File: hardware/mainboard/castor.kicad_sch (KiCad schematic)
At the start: 46 parts, among them J116 OSC, Q1 MMBT3906, U3 TL074, U4 74LVC2G74, U5 MCP6001-OT, U6 TL074

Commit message: Cleanup MCU schematic
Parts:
- C11: Reqs audio path, 20v -> audio path, low-voltage (3.3V), 16V; finalized yes & alt -> (none); mpn CL21A106KAYNNN -> (none); mpn alt CL21A106KAFN3NE -> (none); mpn specs 10% 25v -> (none)
- C12: Reqs audio path, 20v -> audio path, low-voltage (3.3V), 16V; finalized yes & alt -> no; mpn CL21A106KAYNNN -> (none); mpn alt CL21A106KAFN3NE -> (none); mpn specs 10% 25v -> (none)
- C13: Reqs audio path, 20v -> audio path, low-voltage (3.3V), 16V; mpn CL21A106KAYNNN -> (none); mpn alt CL21A106KAFN3NE -> (none); mpn specs 10% 25v -> (none)
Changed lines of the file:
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@@
     (rev "v5")
     (company "Winterbloom")
-    (comment 1 "CERN-OHL-P v2")
-    (comment 2 "Alethea Flowers")
+    (comment 1 "Alethea Flowers")
+    (comment 2 "CERN-OHL-P v2")
+    (comment 3 "gemini.wntr.dev")
   )
   (junction (at 207.01 111.76) (diameter 0) (color 0 0 0 0)
@@
       (effects (font (size 1.27 1.27)) hide)
     )
-    (property "finalized" "yes & alt" (id 4) (at 203.835 45.72 0)
-      (effects (font (size 1.27 1.27)) hide)
-    )
-    (property "mpn" "CL21A106KAYNNN" (id 5) (at 203.835 45.72 0)
-      (effects (font (size 1.27 1.27)) hide)
-    )
-    (property "mpn specs" "10% 25v" (id 6) (at 203.835 45.72 0)
-      (effects (font (size 1.27 1.27)) hide)
-    )
-    (property "mpn alt" "CL21A106KAFN3NE" (id 7) (at 203.835 45.72 0)
-      (effects (font (size 1.27 1.27)) hide)
-    )
-    (property "Reqs" "audio path, 20v" (id 8) (at 203.835 45.72 0)
+    (property "finalized" "" (id 4) (at 203.835 45.72 0)
+      (effects (font (size 1.27 1.27)) hide)
+    )
+    (property "mpn" "" (id 5) (at 203.835 45.72 0)
+      (effects (font (size 1.27 1.27)) hide)
+    )
+    (property "mpn specs" "" (id 6) (at 203.835 45.72 0)
+      (effects (font (size 1.27 1.27)) hide)
+    )
+    (property "mpn alt" "" (id 7) (at 203.835 45.72 0)
+      (effects (font (size 1.27 1.27)) hide)
+    )
+    (property "Reqs" "audio path, low-voltage (3.3V), 16V" (id 8) (at 203.835 45.72 0)
       (effects (font (size 1.27 1.27)) hide)
     )
@@
       (effects (font (size 1.27 1.27)) hide)
     )
-    (property "mpn" "CL21A106KAYNNN" (id 5) (at 203.2 78.74 0)
-      (effects (font (size 1.27 1.27)) hide)
-    )
-    (property "mpn specs" "10% 25v" (id 6) (at 203.2 78.74 0)
-      (effects (font (size 1.27 1.27)) hide)
-    )
-    (property "mpn alt" "CL21A106KAFN3NE" (id 7) (at 203.2 78.74 0)
-      (effects (font (size 1.27 1.27)) hide)
-    )
-    (property "Reqs" "audio path, 20v" (id 8) (at 203.2 78.74 0)
+    (property "mpn" "" (id 5) (at 203.2 78.74 0)
+      (effects (font (size 1.27 1.27)) hide)
+    )
+    (property "mpn specs" "" (id 6) (at 203.2 78.74 0)
+      (effects (font (size 1.27 1.27)) hide)
+    )
+    (property "mpn alt" "" (id 7) (at 203.2 78.74 0)
+      (effects (font (size 1.27 1.27)) hide)
+    )
+    (property "Reqs" "audio path, low-voltage (3.3V), 16V" (id 8) (at 203.2 78.74 0)
       (effects (font (size 1.27 1.27)) hide)
     )
@@
       (effects (font (size 1.27 1.27)) hide)
     )
-    (property "finalized" "yes & alt" (id 4) (at 203.2 111.76 0)
-      (effects (font (size 1.27 1.27)) hide)
-    )
-    (property "mpn" "CL21A106KAYNNN" (id 5) (at 203.2 111.76 0)
-      (effects (font (size 1.27 1.27)) hide)
-    )
-    (property "mpn specs" "10% 25v" (id 6) (at 203.2 111.76 0)
-      (effects (font (size 1.27 1.27)) hide)
-    )
-    (property "mpn alt" "CL21A106KAFN3NE" (id 7) (at 203.2 111.76 0)
-      (effects (font (size 1.27 1.27)) hide)
-    )
-    (property "Reqs" "audio path, 20v" (id 8) (at 203.2 111.76 0)
-      (effects (font (size 1.27 1.27)) hide)
-    )
+    (property "finalized" "no" (id 4) (at 203.2 111.76 0)
+      (effects (font (size 1.27 1.27)) hide)
+    )
+    (property "mpn" "" (id 5) (at 203.2 111.76 0)
+      (effects (font (size 1.27 1.27)) hide)
+    )
+    (property "mpn specs" "" (id 6) (at 203.2 111.76 0)
+      (effects (font (size 1.27 1.27)) hide)
+    )
+    (property "mpn alt" "" (id 7) (at 203.2 111.76 0)
+      (effects (font (size 1.27 1.27)) hide)
+    )
+    (property "Reqs" "audio path, low-voltage (3.3V), 16V" (id 8) (at 203.2 111.76 0)
+      (effects (font (size 1.27 1.27)) hide)
+    )

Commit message: More schematic cleanup - nearly done!
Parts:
- J116: value OSC -> OSC OUT
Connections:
- net PULSE renamed PULSE_OUT
- net RAMP renamed RAMP_OUT
- net SUB renamed SUB_OUT
- net charge_cv_in renamed CHARGE_CV_IN
- net mix_out renamed MIX_OUT
- net pwm_cv_in renamed PWM_CV_IN
- net square_in renamed SQUARE_IN
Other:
- moved on the sheet: C11, C12, C13, C14, C15, C16, R10, R11, R12, R13, R14, R15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

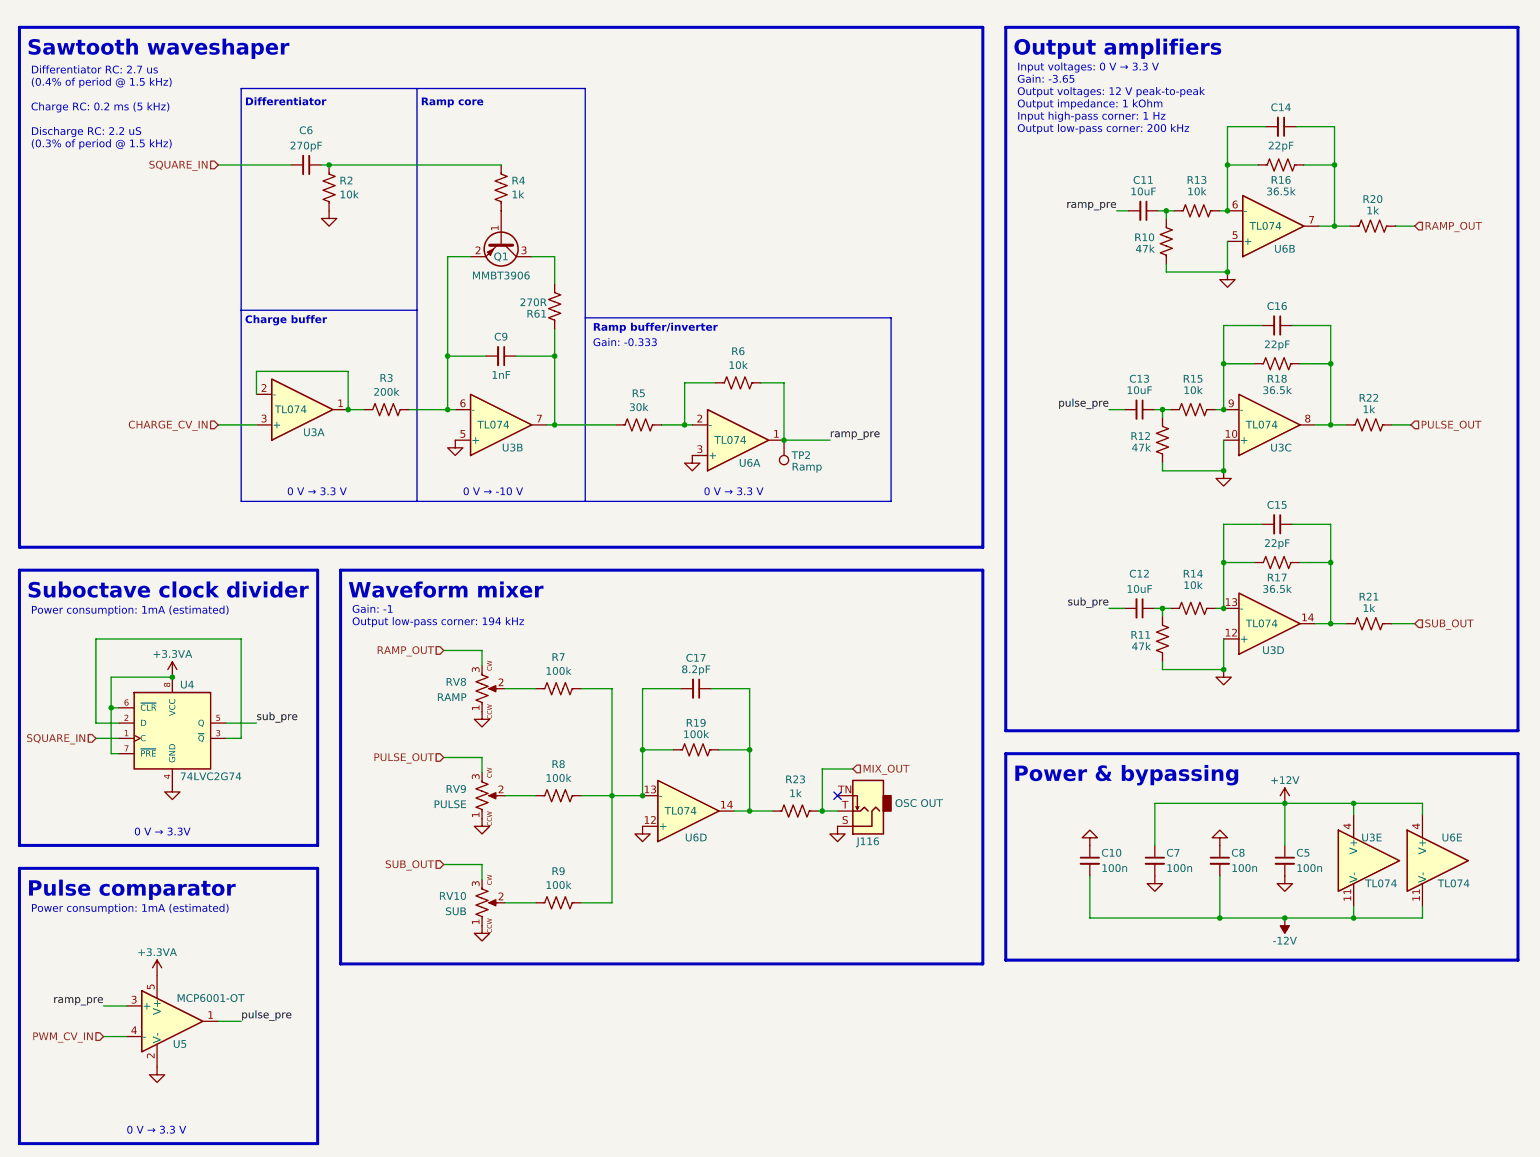
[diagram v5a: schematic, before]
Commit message: Reannotate schematic
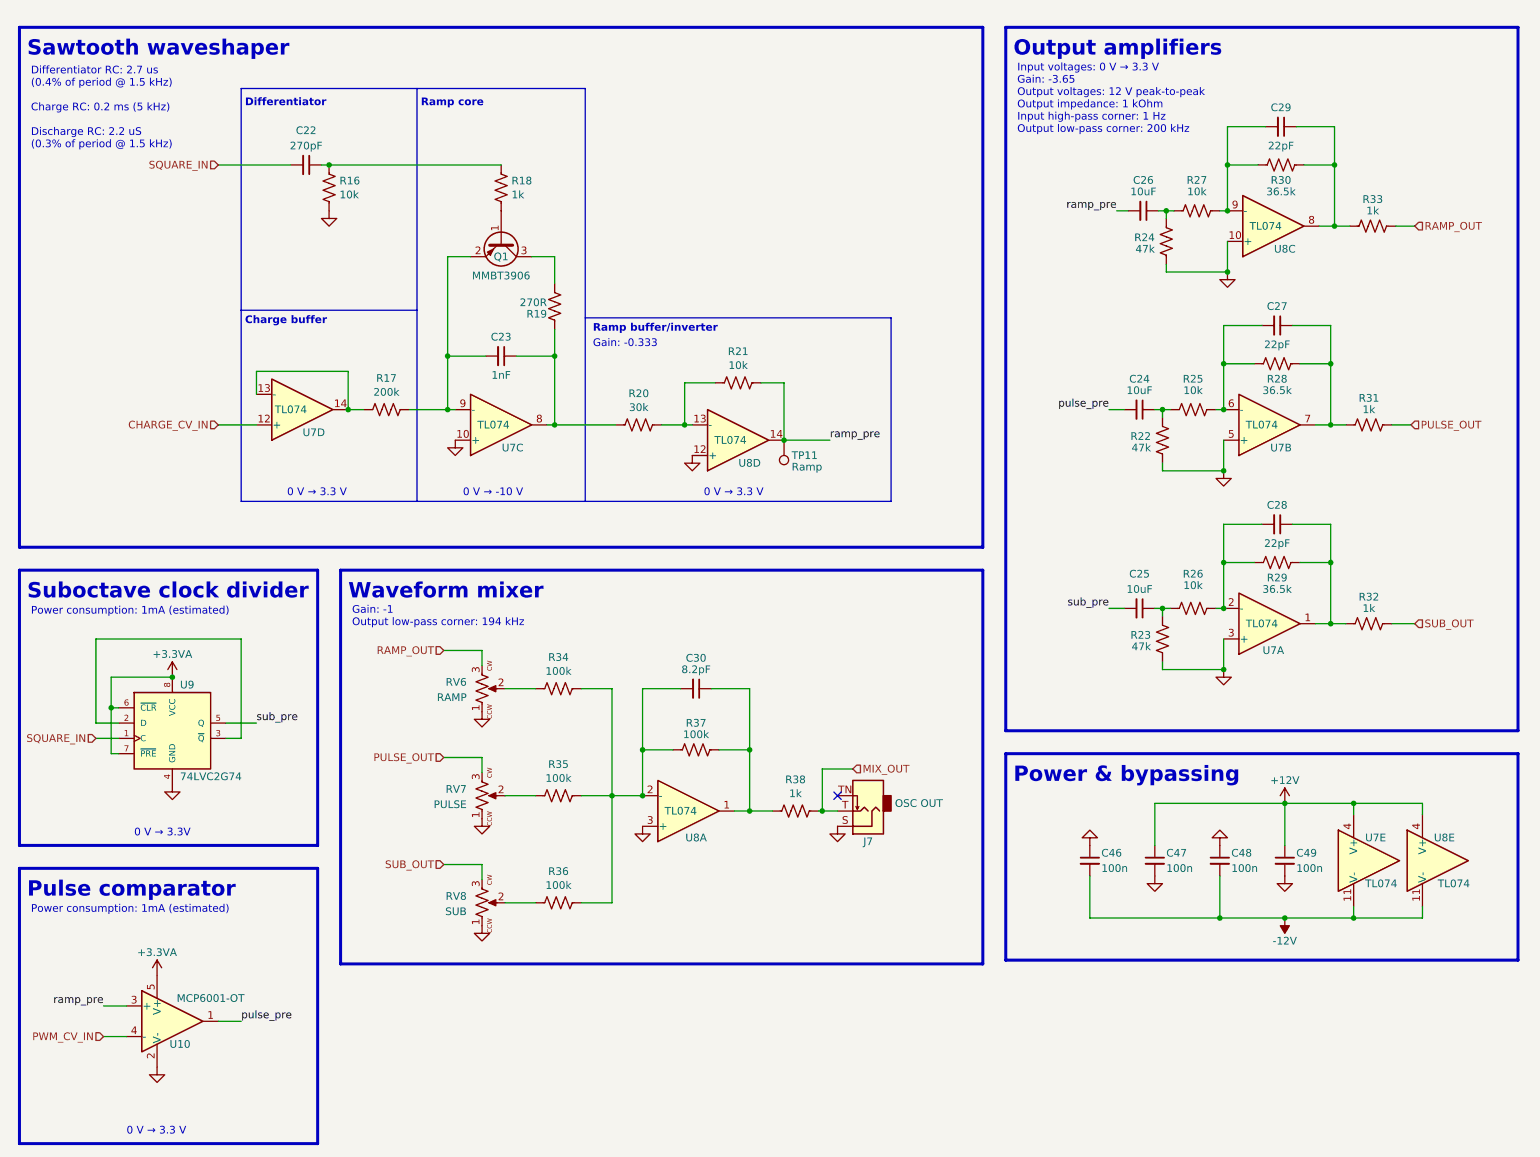
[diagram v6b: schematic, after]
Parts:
- renumbered C6 to C22, C9 to C23, C13 to C24, C12 to C25, C11 to C26, C16 to C27, C15 to C28, C14 to C29, C17 to C30, C10 to C46, C7 to C47, C8 to C48, C5 to C49, J116 to J7, R2 to R16, R3 to R17, R4 to R18, R61 to R19, R5 to R20, R6 to R21, R12 to R22, R11 to R23, R10 to R24, R15 to R25, R14 to R26, R13 to R27, R18 to R28, R17 to R29, R16 to R30, R22 to R31, R21 to R32, R20 to R33, R7 to R34, R8 to R35, R9 to R36, R19 to R37, R23 to R38, RV8 to RV6, RV9 to RV7, RV10 to RV8, TP2 to TP11, U5 to U10, U3 to U7, U6 to U8, U4 to U9
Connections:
- net CHARGE_CV_IN: now also U7.12 (+); no longer U7.3 (+)
- net GND: now also U7.10 (+), U7.3 (+), U7.5 (+), U8.10 (+), U8.12 (+), U8.3 (+); no longer U7.10 (+), U7.12 (+), U7.5 (+), U8.12 (+), U8.3 (+), U8.5 (+)
- net ramp_pre: now also U8.14; no longer U8.1
- net at C23.2, Q1.2 (E), R17.2: now also U7.9 (-); no longer U7.6 (-)
- net at C23.1, R19.1, R20.1: now also U7.8; no longer U7.7
- net at R20.2, R21.1: now also U8.13 (-); no longer U8.2 (-)
- net at C29.2, R27.2, R30.1: now also U8.9 (-); no longer U8.6 (-)
- net at C29.1, R30.2, R33.1: now also U8.8; no longer U8.7
- net at C30.2, R34.2, R35.2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: now also U8.2 (-); no longer U8.13 (-)
- net at C30.1, R37.2, R38.1: now also U8.1; no longer U8.14
- net at C27.2, R25.2, R28.1: now also U7.6 (-); no longer U7.9 (-)
- net at C27.1, R28.2, R31.1: now also U7.7; no longer U7.8
- net at C28.2, R26.2, R29.1: now also U7.2 (-); no longer U7.13 (-)
- net at C28.1, R29.2, R32.1: now also U7.1; no longer U7.14
- new net: R17.1, U7.13 (-), U7.14

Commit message: Normalize component values
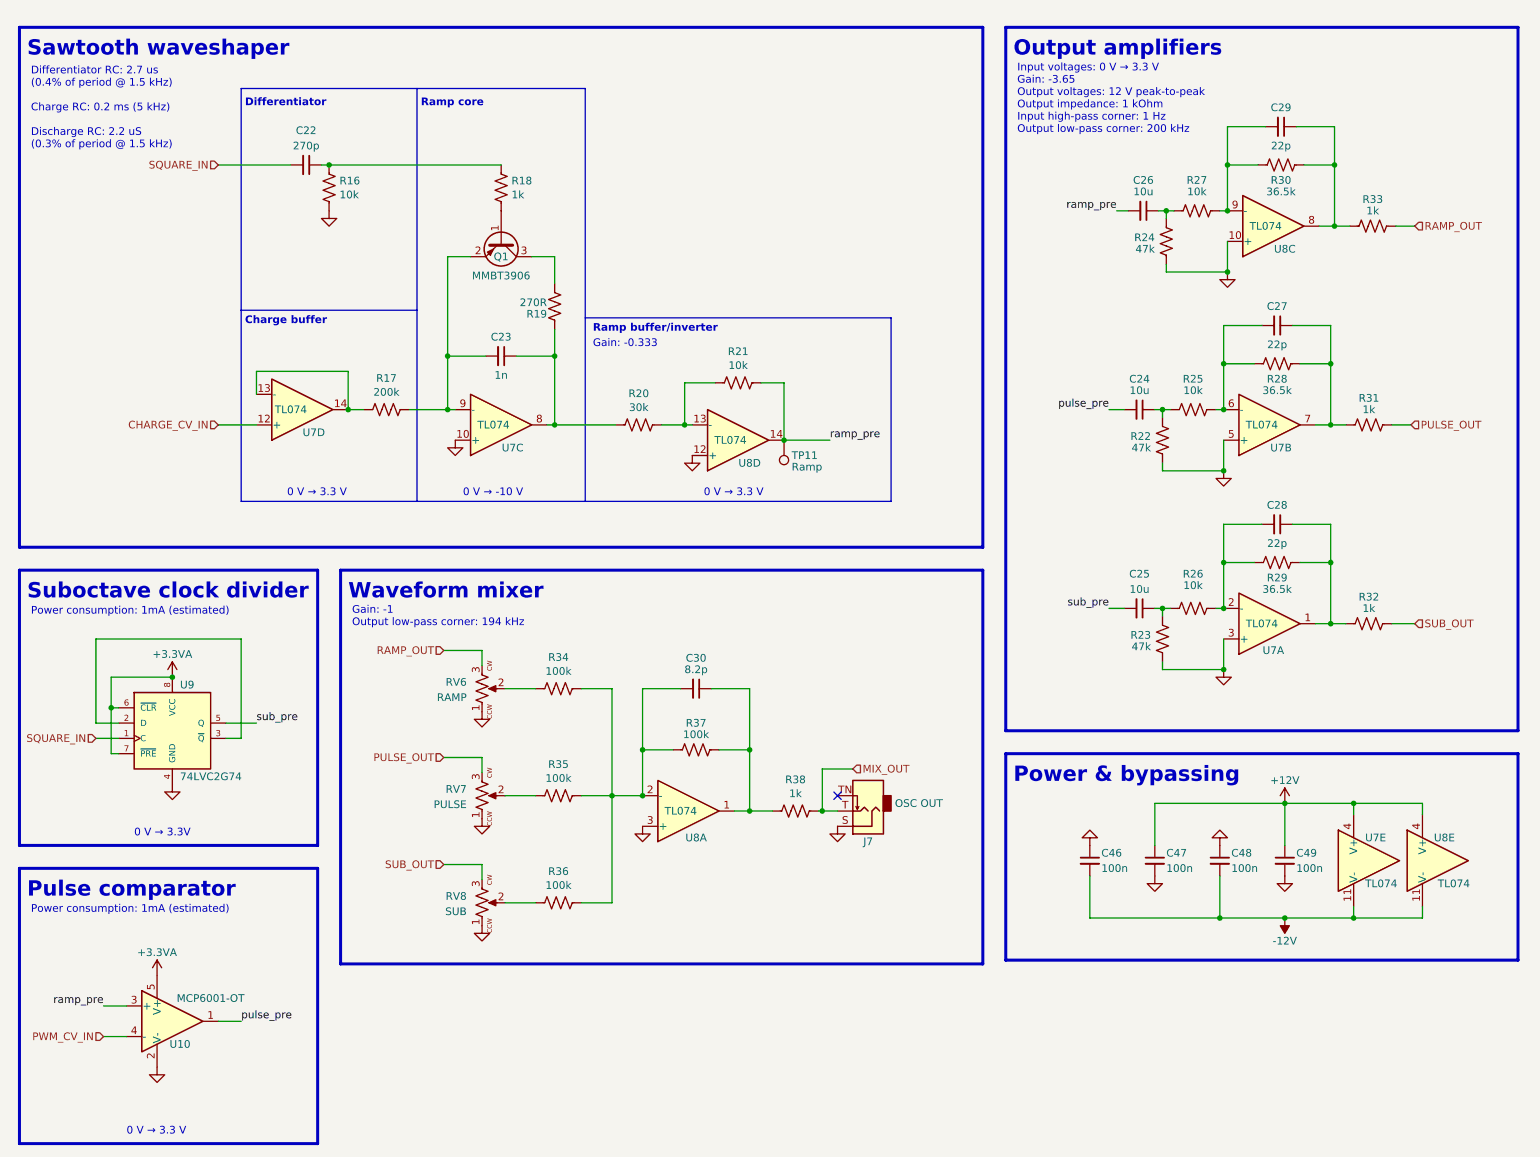
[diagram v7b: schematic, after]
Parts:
- C22: value 270pF -> 270p
- C23: value 1nF -> 1n
- C24, C25, C26: value 10uF -> 10u
- C27, C28, C29: value 22pF -> 22p
- C30: value 8.2pF -> 8.2p
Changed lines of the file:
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@@
     (in_bom yes) (on_board yes)
     (property "Reference" "C22" (id 0) (at 62.865 32.385 90))
-    (property "Value" "270pF" (id 1) (at 62.865 34.925 90))
+    (property "Value" "270p" (id 1) (at 62.865 34.925 90))
     (property "Footprint" "Capacitor_SMD:C_0402_1005Metric_Pad0.74x0.62mm_HandSolder" (id 2) (at 59.055 39.0652 0)
       (effects (font (size 1.27 1.27)) hide)
@@
     (in_bom yes) (on_board yes)
     (property "Reference" "C23" (id 0) (at 95.25 66.675 90))
-    (property "Value" "1nF" (id 1) (at 95.25 73.025 90))
+    (property "Value" "1n" (id 1) (at 95.25 73.025 90))
     (property "Footprint" "Capacitor_SMD:C_0402_1005Metric_Pad0.74x0.62mm_HandSolder" (id 2) (at 91.44 70.8152 0)
       (effects (font (size 1.27 1.27)) hide)
@@
     (in_bom yes) (on_board yes)
     (property "Reference" "C26" (id 0) (at 201.93 40.64 90))
-    (property "Value" "10uF" (id 1) (at 201.93 42.545 90))
+    (property "Value" "10u" (id 1) (at 201.93 42.545 90))
     (property "Footprint" "Capacitor_SMD:C_0805_2012Metric_Pad1.18x1.45mm_HandSolder" (id 2) (at 198.12 46.6852 0)
       (effects (font (size 1.27 1.27)) hide)
@@
     (in_bom yes) (on_board yes)
     (property "Reference" "C29" (id 0) (at 224.79 28.575 90))
-    (property "Value" "22pF" (id 1) (at 224.79 34.925 90))
+    (property "Value" "22p" (id 1) (at 224.79 34.925 90))
     (property "Footprint" "Capacitor_SMD:C_0402_1005Metric_Pad0.74x0.62mm_HandSolder" (id 2) (at 220.98 32.7152 0)
       (effects (font (size 1.27 1.27)) hide)
@@
     (in_bom yes) (on_board yes)
     (property "Reference" "C24" (id 0) (at 201.295 73.66 90))
-    (property "Value" "10uF" (id 1) (at 201.295 75.565 90))
+    (property "Value" "10u" (id 1) (at 201.295 75.565 90))
     (property "Footprint" "Capacitor_SMD:C_0805_2012Metric_Pad1.18x1.45mm_HandSolder" (id 2) (at 197.485 79.7052 0)
       (effects (font (size 1.27 1.27)) hide)
@@
     (in_bom yes) (on_board yes)
     (property "Reference" "C27" (id 0) (at 224.155 61.595 90))
-    (property "Value" "22pF" (id 1) (at 224.155 67.945 90))
+    (property "Value" "22p" (id 1) (at 224.155 67.945 90))
     (property "Footprint" "Capacitor_SMD:C_0402_1005Metric_Pad0.74x0.62mm_HandSolder" (id 2) (at 220.345 65.7352 0)
       (effects (font (size 1.27 1.27)) hide)
@@
     (in_bom yes) (on_board yes)
     (property "Reference" "C25" (id 0) (at 201.295 106.045 90))
-    (property "Value" "10uF" (id 1) (at 201.295 108.585 90))
+    (property "Value" "10u" (id 1) (at 201.295 108.585 90))
     (property "Footprint" "Capacitor_SMD:C_0805_2012Metric_Pad1.18x1.45mm_HandSolder" (id 2) (at 197.485 112.7252 0)
       (effects (font (size 1.27 1.27)) hide)
@@
     (in_bom yes) (on_board yes)
     (property "Reference" "C28" (id 0) (at 224.155 94.615 90))
-    (property "Value" "22pF" (id 1) (at 224.155 100.965 90))
+    (property "Value" "22p" (id 1) (at 224.155 100.965 90))
     (property "Footprint" "Capacitor_SMD:C_0402_1005Metric_Pad0.74x0.62mm_HandSolder" (id 2) (at 220.345 98.7552 0)
       (effects (font (size 1.27 1.27)) hide)
@@
     (in_bom yes) (on_board yes)
     (property "Reference" "C30" (id 0) (at 127.635 120.015 90))
-    (property "Value" "8.2pF" (id 1) (at 127.635 121.92 90))
+    (property "Value" "8.2p" (id 1) (at 127.635 121.92 90))
     (property "Footprint" "Capacitor_SMD:C_0402_1005Metric_Pad0.74x0.62mm_HandSolder" (id 2) (at 123.825 126.0602 0)
       (effects (font (size 1.27 1.27)) hide)
